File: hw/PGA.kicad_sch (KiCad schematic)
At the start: 16 parts, among them U1401 MAX9939AUB+T

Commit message: Checkpoint reverting away from VLF extension
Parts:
- added C1410: 10uF, Capacitor_SMD:C_0603_1608Metric, symbol Device:C_US
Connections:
- net +2V5bias: now also C1410.1
- net GND: now also C1410.2

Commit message: Preparing to take another swing at layout for rf200. I THINK the previous gaffes have been repaired elsewhere - cause by BOM machinations and my clumsiness.
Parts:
- C1401, C1402: JLCPCBpn (none) -> C170182
- C1403, C1405: JLCPCBpn (none) -> C24452
- C1404: JLCPCBpn (none) -> C301928
- C1406, C1407: JLCPCBpn (none) -> C107038
- C1408, C1409: JLCPCBpn (none) -> C107048
- C1410: JLCPCBpn (none) -> C327087; Manufacturer_Name (none) -> Taoup Uidem; Manufacturer_Part_Number (none) -> 81-GXT155R71E223KE1D; Mouser Part Number (none) -> 963-MLAST168BB5106MT; working-voltage (none) -> 25V
- U1401: JLCPCBpn (none) -> C2057611
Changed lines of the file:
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@@
 			)
 		)
-		(property "JLCPCBpn" ""
+		(property "JLCPCBpn" "C107048"
 			(at 180.34 73.66 0)
 			(effects
@@
 			)
 		)
-		(property "JLCPCBpn" ""
+		(property "JLCPCBpn" "C107038"
 			(at 160.02 76.2 0)
 			(effects
@@
 			)
 		)
-		(property "JLCPCBpn" ""
+		(property "JLCPCBpn" "C107038"
 			(at 160.02 92.71 0)
 			(effects
@@
 			)
 		)
-		(property "JLCPCBpn" ""
+		(property "JLCPCBpn" "C107048"
 			(at 180.34 106.68 0)
 			(effects
@@
 			)
 		)
-		(property "JLCPCBpn" ""
+		(property "JLCPCBpn" "C24452"
 			(at 97.79 99.06 0)
 			(effects
@@
 			)
 		)
-		(property "JLCPCBpn" ""
+		(property "JLCPCBpn" "C170182"
 			(at 62.23 76.2 0)
 			(effects
@@
 			)
 		)
+		(property "JLCPCBpn" "C327087"
+			(at 91.44 62.23 0)
+			(effects
+				(font
+					(size 1.27 1.27)
+				)
+				(hide yes)
+			)
+		)
+		(property "Manufacturer_Name" "Taoup Uidem"
+			(at 91.44 62.23 0)
+			(effects
+				(font
+					(size 1.27 1.27)
+				)
+				(hide yes)
+			)
+		)
+		(property "Manufacturer_Part_Number" "81-GXT155R71E223KE1D"
+			(at 91.44 62.23 0)
+			(effects
+				(font
+					(size 1.27 1.27)
+				)
+				(hide yes)
+			)
+		)
+		(property "Mouser Part Number" "963-MLAST168BB5106MT"
+			(at 91.44 62.23 0)
+			(effects
+				(font
+					(size 1.27 1.27)
+				)
+				(hide yes)
+			)
+		)
+		(property "working-voltage" "25V"
+			(at 91.44 62.23 0)
+			(effects
+				(font
+					(size 1.27 1.27)
+				)
+				(hide yes)
+			)
+		)
 		(pin "1"
 		)
@@
 			)
 		)
-		(property "JLCPCBpn" ""
+		(property "JLCPCBpn" "C170182"
 			(at 57.15 78.74 0)
 			(effects
@@
 			)
 		)
-		(property "JLCPCBpn" ""
+		(property "JLCPCBpn" "C301928"
 			(at 92.71 99.06 0)
 			(effects
@@
 			)
 		)
-		(property "JLCPCBpn" ""
+		(property "JLCPCBpn" "C2057611"
 			(at 106.68 68.58 0)
 			(effects
@@
 			)
 		)
-		(property "JLCPCBpn" ""
+		(property "JLCPCBpn" "C24452"
 			(at 82.55 62.23 0)
 			(effects

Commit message: I think I have a valid BOM with JLCPCB part numbers for everything now
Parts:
- R1401, R1402, R1403, R1404: JLCPCBpn (none) -> C723366
- R1405, R1406: footprint Resistor_SMD:R_0603_1608Metric -> Resistor_SMD:R_0402_1005Metric; JLCPCBpn (none) -> C854274
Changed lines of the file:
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@@
 			)
 		)
-		(property "JLCPCBpn" ""
+		(property "JLCPCBpn" "C723366"
 			(at 166.37 76.2 90)
 			(effects
@@
 			)
 		)
-		(property "Footprint" "Resistor_SMD:R_0603_1608Metric"
+		(property "Footprint" "Resistor_SMD:R_0402_1005Metric"
 			(at 174.244 102.616 90)
 			(effects
@@
 			)
 		)
-		(property "JLCPCBpn" ""
+		(property "JLCPCBpn" "C854274"
 			(at 173.99 101.6 90)
 			(effects
@@
 			)
 		)
-		(property "JLCPCBpn" ""
+		(property "JLCPCBpn" "C723366"
 			(at 71.12 63.5 90)
 			(effects
@@
 			)
 		)
-		(property "JLCPCBpn" ""
+		(property "JLCPCBpn" "C723366"
 			(at 166.37 92.71 90)
 			(effects
@@
 			)
 		)
-		(property "Footprint" "Resistor_SMD:R_0603_1608Metric"
+		(property "Footprint" "Resistor_SMD:R_0402_1005Metric"
 			(at 174.244 69.596 90)
 			(effects
@@
 			)
 		)
-		(property "JLCPCBpn" ""
+		(property "JLCPCBpn" "C854274"
 			(at 173.99 68.58 90)
 			(effects
@@
 			)
 		)
-		(property "JLCPCBpn" ""
+		(property "JLCPCBpn" "C723366"
 			(at 76.2 63.5 90)
 			(effects

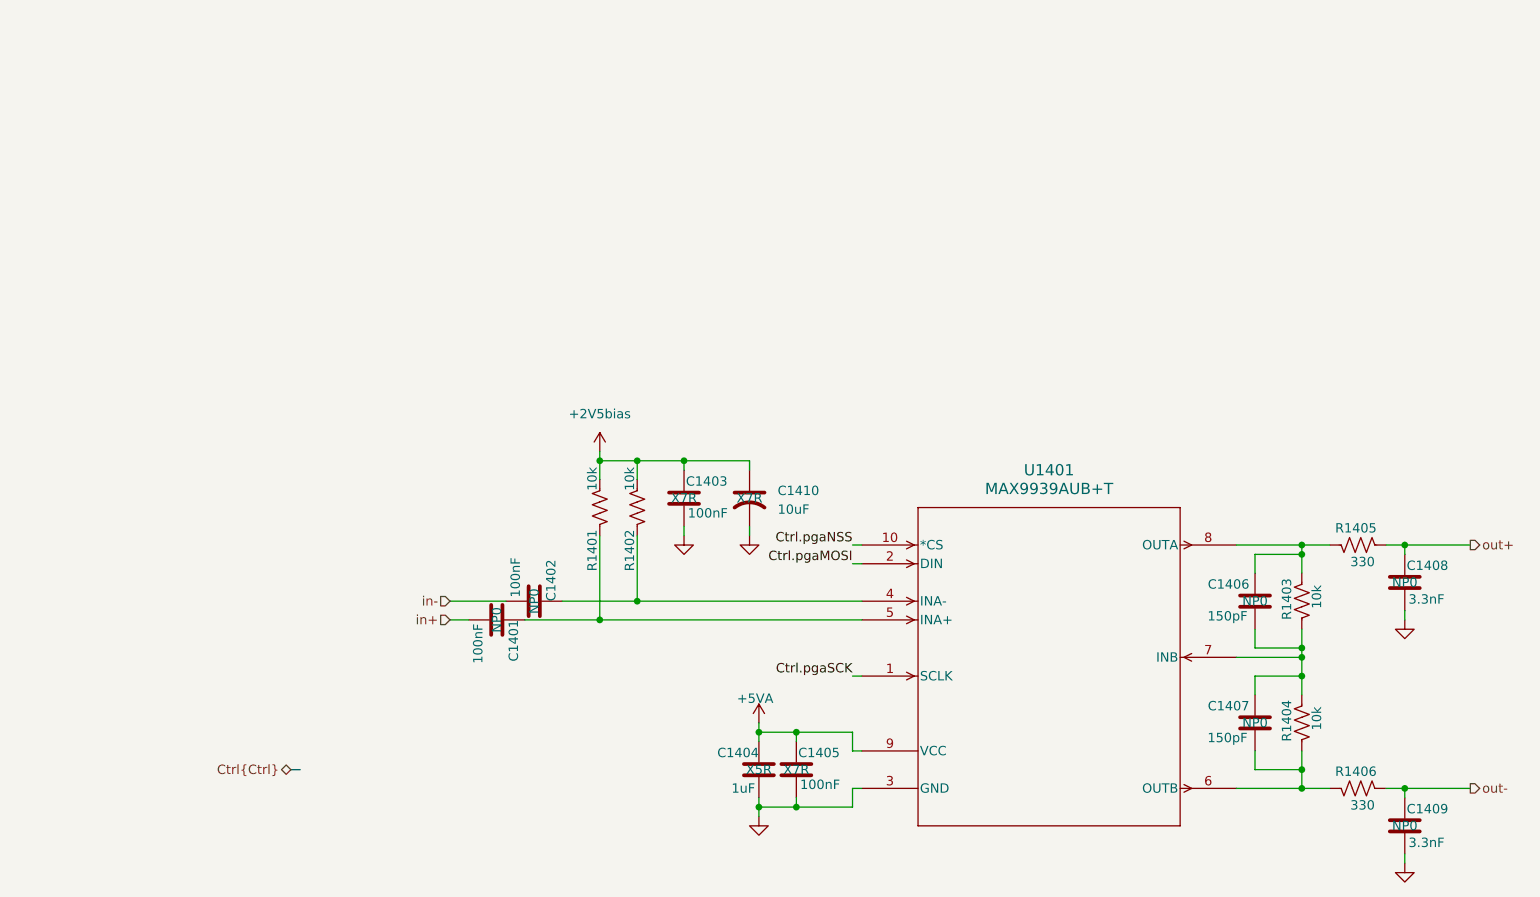
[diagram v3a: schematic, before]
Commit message: Consolidate BOM management and back-propagate properties to schematics
* Implement unified BOM processor (tools/bom-processor.py) using kicad-cli for macro expansion and field collapsing.
* Back-propagate unified component properties (Manufacturer, MPN, LCSC_PN, Mouser_PN, Description) to all KiCad schematic files.
* Generate initial production BOM (production/nexrx-bom.csv) with 100% LCSC part number coverage.
* Standardize passive component descriptions with full technical specifications (dielectric, voltage, tolerance).
* Clean up redundant manufacturer and part number fields in schematic symbols.
* Remove obsolete BOM management scripts.
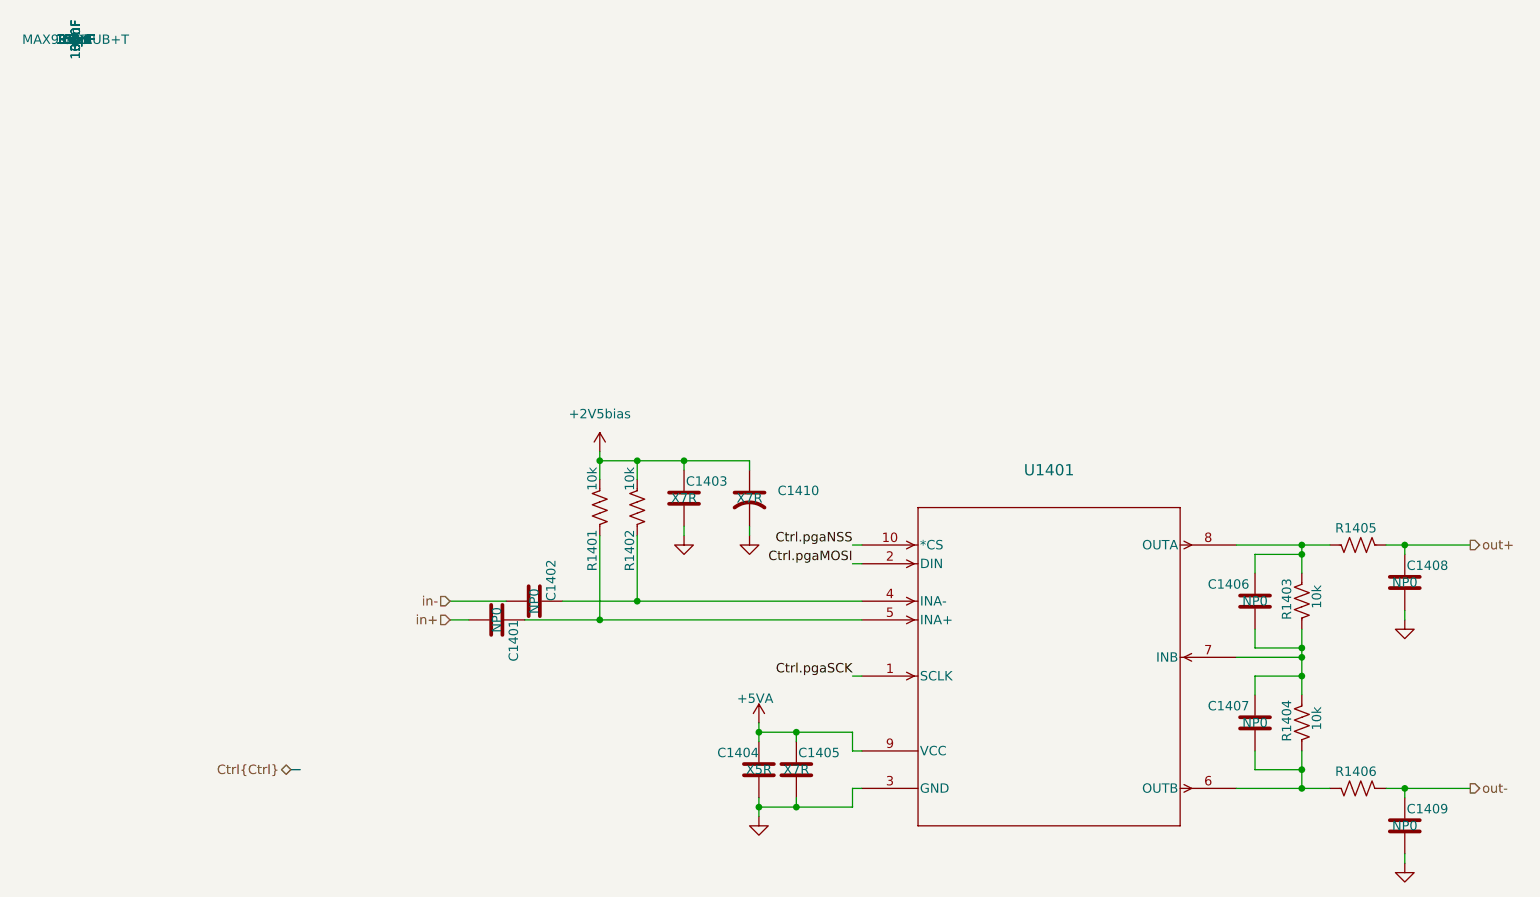
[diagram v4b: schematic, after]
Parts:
- C1401, C1402: JLCPCBpn C170182 -> (none); LCSC_PN (none) -> C170182; MPN (none) -> GRM3195C2A104JA01D; Manufacturer (none) -> Murata; Manufacturer_Name Murata -> (none); Manufacturer_Part_Number GRM31C5C2A104JA01L -> (none); Mouser Part Number 81-GRM31C5C2A104JA1L -> (none); Mouser_PN (none) -> 81-GRM31C5C2A104JA1L
- C1403, C1405: JLCPCBpn C24452 -> (none); LCSC_PN (none) -> C24452; MPN (none) -> C0805F104K1RACAUTO; Manufacturer (none) -> Kemet; Manufacturer_Name Kemet -> (none); Manufacturer_Part_Number C0805F104K1RACAUTO -> (none); Mouser Part Number 80-C0805F104K1RAUTO -> (none); Mouser_PN (none) -> 80-C0805F104K1RAUTO
- C1404: JLCPCBpn C301928 -> (none); LCSC_PN (none) -> C301928; MPN (none) -> GRM155R61E105KE11D; Manufacturer (none) -> Murata; Manufacturer_Name Murata -> (none); Manufacturer_Part_Number GRM155R61E105KE11D -> (none); Mouser Part Number 81-GRM155R61E105KE1D -> (none); Mouser_PN (none) -> 81-GRM155R61E105KE1D
- C1406, C1407: JLCPCBpn C107038 -> (none); LCSC_PN (none) -> C107038; MPN (none) -> 06033A151FAT2A; Manufacturer (none) -> Kyocera AVX; Manufacturer_Name Kyocera AVX -> (none); Manufacturer_Part_Number 06033A151FAT2A -> (none); Mouser Part Number 581-06033A151FAT2A -> (none); Mouser_PN (none) -> 581-06033A151FAT2A
- C1408, C1409: JLCPCBpn C107048 -> (none); LCSC_PN (none) -> C107048; MPN (none) -> C1608C0G1H332J080AE; Manufacturer (none) -> TDK; Manufacturer_Name TDK -> (none); Manufacturer_Part_Number C1608C0G1H332J080AE -> (none); Mouser Part Number 810-C1608C0G1H332J08 -> (none); Mouser_PN (none) -> 810-C1608C0G1H332J08
- C1410: JLCPCBpn C327087 -> (none); LCSC_PN (none) -> C327087; MPN (none) -> 81-GXT155R71E223KE1D; Manufacturer (none) -> Taoup Uidem; Manufacturer_Name Taoup Uidem -> (none); Manufacturer_Part_Number 81-GXT155R71E223KE1D -> (none); Mouser Part Number 963-MLAST168BB5106MT -> (none); Mouser_PN (none) -> 963-MLAST168BB5106MT
- R1405, R1406: JLCPCBpn C854274 -> (none); LCSC_PN (none) -> C854274
- U1401: JLCPCBpn C2057611 -> (none); LCSC_PN (none) -> C2057611
